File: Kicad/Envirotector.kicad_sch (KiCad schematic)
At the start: 3 parts, among them J1 OLED Display, U1 XIAO-RP2040-DIP, U2 DHT11

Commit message: Upload
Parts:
- added J2: Micro_SD_Card, Connector_Card:microSD_HC_Hirose_DM3AT-SF-PEJM5, symbol Connector:Micro_SD_Card
- added SW1: RotaryEncoder_Switch, Rotary_Encoder:RotaryEncoder_Alps_EC11E-Switch_Vertical_H20mm, symbol Device:RotaryEncoder_Switch
- added U3: ~, LARGE:RTC_DS3231, symbol RTC:RTC_DS3231
- added U4: ~, SPARK:BMP180, symbol BMP:BMP180
- U1: footprint OPL:XIAO-RP2040-DIP -> Module:MOUDLE14P-XIAO-DIP-SMD
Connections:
- net +3.3V: now also J2.4 (VDD), U4.2 (VCC)
- net +5V: now also U3.3 (VCC)
- net GND: now also J2.6 (VSS), J2.9 (SHIELD), SW1.C, SW1.S1, U3.4 (GND), U4.7 (GND)
- net at J1.1 (Pin_1), U1.5 (GPIO6/SDA): now also U3.2 (SDA), U4.6 (SDA)
- net at J1.2 (Pin_2), U1.6 (GPIO7/SCL): now also U3.1 (SCL), U4.5 (SCL)
- net at U1.1 (GPIO26/ADC0/A0): now also J2.2 (DAT3/CD); no longer U2.2 (DATA)
- net at U1.10 (GPIO4/MISO): now also J2.7 (DAT0)
- net at U1.11 (GPIO3/MOSI): now also J2.3 (CMD)
- net at U1.2 (GPIO27/ADC1/A1): now also SW1.S2
- net at U1.3 (GPIO28/ADC2/A2): now also SW1.A
- net at U1.4 (GPIO29/ADC3/A3): now also SW1.B
- net at U1.7 (GPIO0/TX): now also U2.2 (DATA)
- net at U1.9 (GPIO2/SCK): now also J2.5 (CLK)

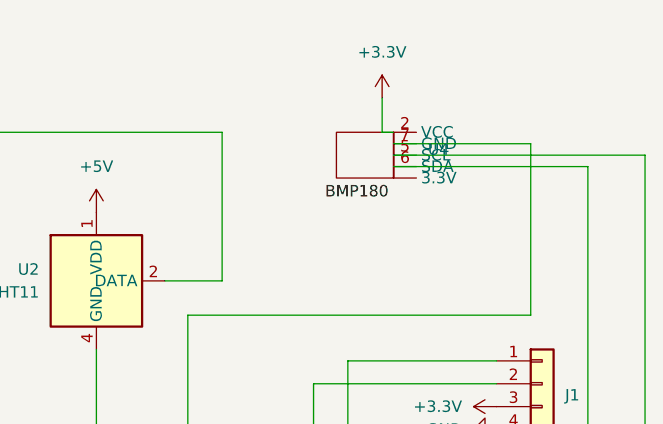
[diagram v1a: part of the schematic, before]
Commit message: updated footprint and case for bmp180 breakout board
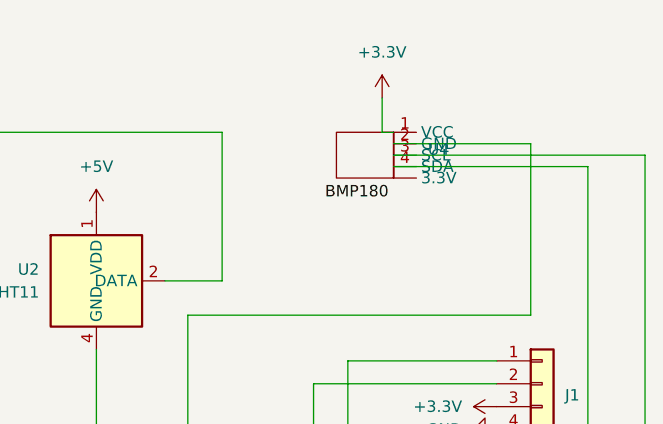
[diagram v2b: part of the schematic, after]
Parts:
- U4: footprint SPARK:BMP180 -> SPARK:Untitled
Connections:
- net +3.3V: now also U4.1 (VCC); no longer U4.2 (VCC)
- net GND: now also U4.2 (GND); no longer U4.7 (GND)
- net at J1.1 (Pin_1), U1.5 (GPIO6/SDA), U3.2 (SDA): now also U4.4 (SDA); no longer U4.6 (SDA)
- net at J1.2 (Pin_2), U1.6 (GPIO7/SCL), U3.1 (SCL): now also U4.3 (SCL); no longer U4.5 (SCL)
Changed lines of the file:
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@@
 			)
 		)
-		(property "Footprint" "SPARK:BMP180"
+		(property "Footprint" "SPARK:Untitled"
 			(at 208.28 38.1 0)
 			(effects
@@
 			)
 		)
-		(pin "5"
+		(pin "1"
 		)
-		(pin "6"
+		(pin "4"
 		)
 		(pin "2"
 		)
-		(pin "7"
+		(pin "3"
 		)
 		(pin ""

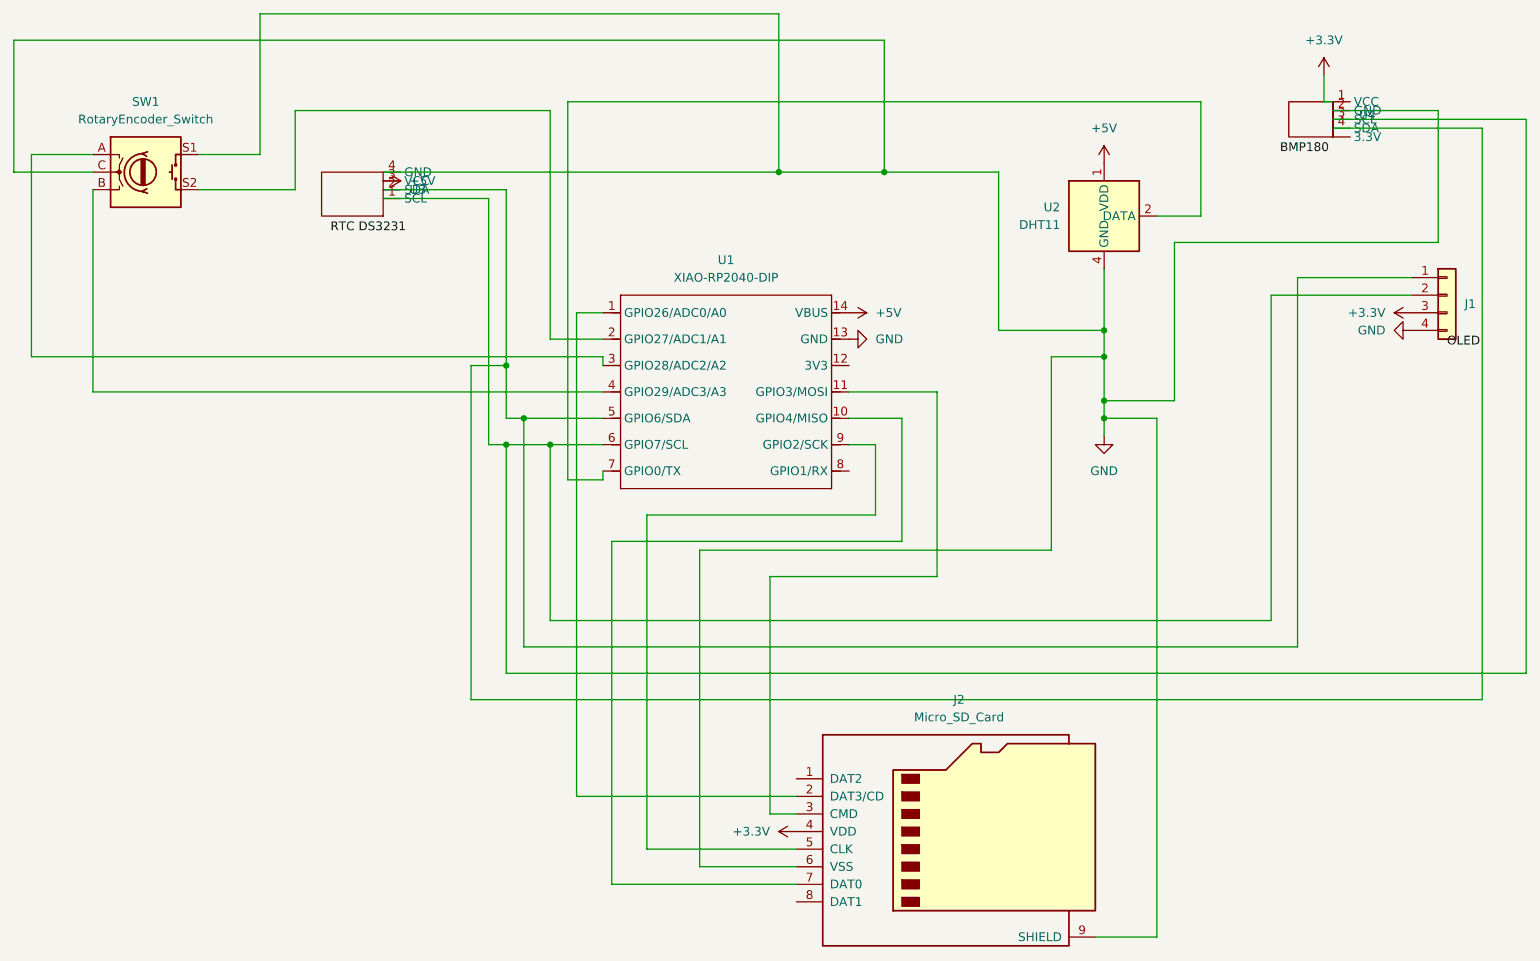
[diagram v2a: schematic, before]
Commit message: updated the sd card reader to breakoutboard
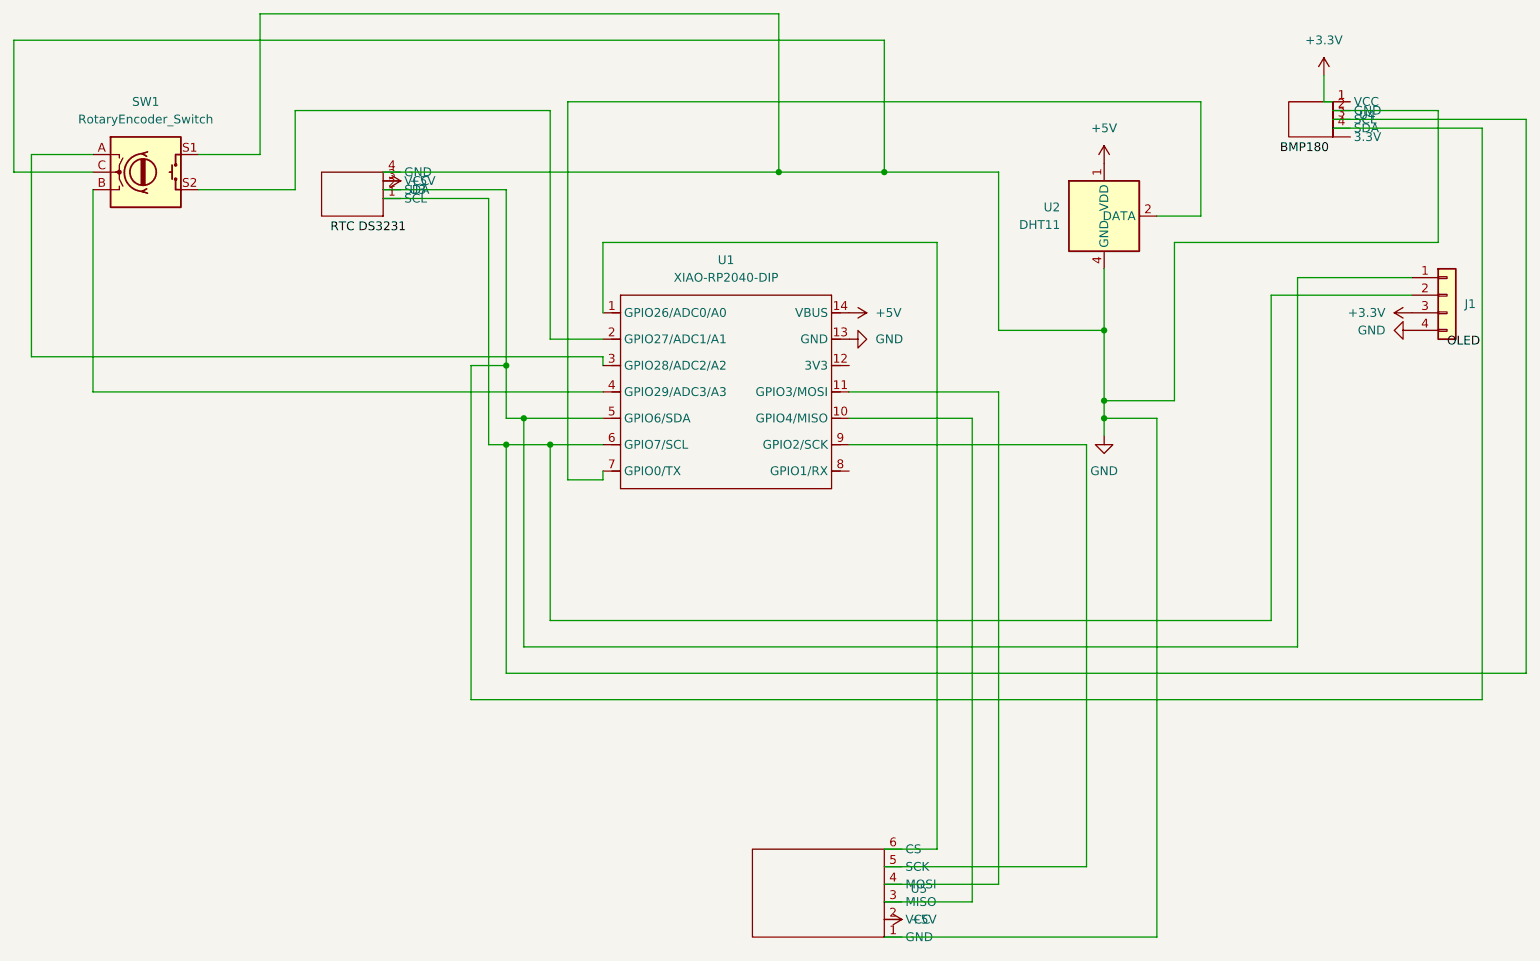
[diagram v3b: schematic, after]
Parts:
- removed J2: Micro_SD_Card, Connector_Card:microSD_HC_Hirose_DM3AT-SF-PEJM5, symbol Connector:Micro_SD_Card
- added U5: ~, SDReader:Untitled, symbol SDReader:SDReader
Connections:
- net +5V: now also U5.2 (VCC)
- net GND: now also U5.1 (GND)
- net at U1.1 (GPIO26/ADC0/A0): now also U5.6 (CS)
- net at U1.11 (GPIO3/MOSI): now also U5.4 (MOSI)
- net at U1.9 (GPIO2/SCK): now also U5.5 (SCK)
- net at U1.10 (GPIO4/MISO): now also U5.3 (MISO)

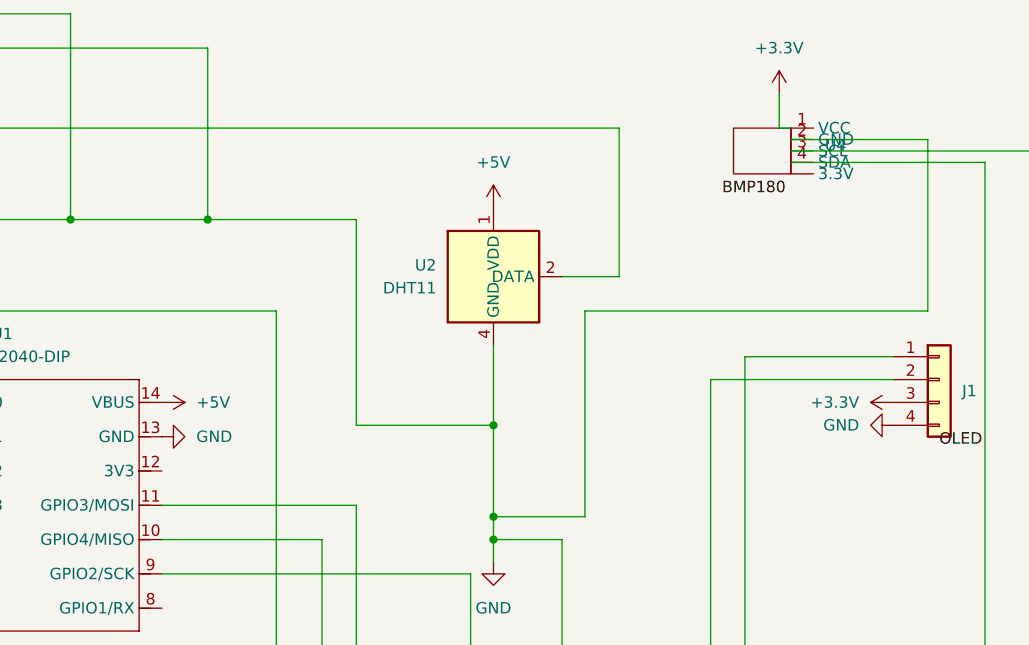
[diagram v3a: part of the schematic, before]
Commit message: updated 3.3v xiao output
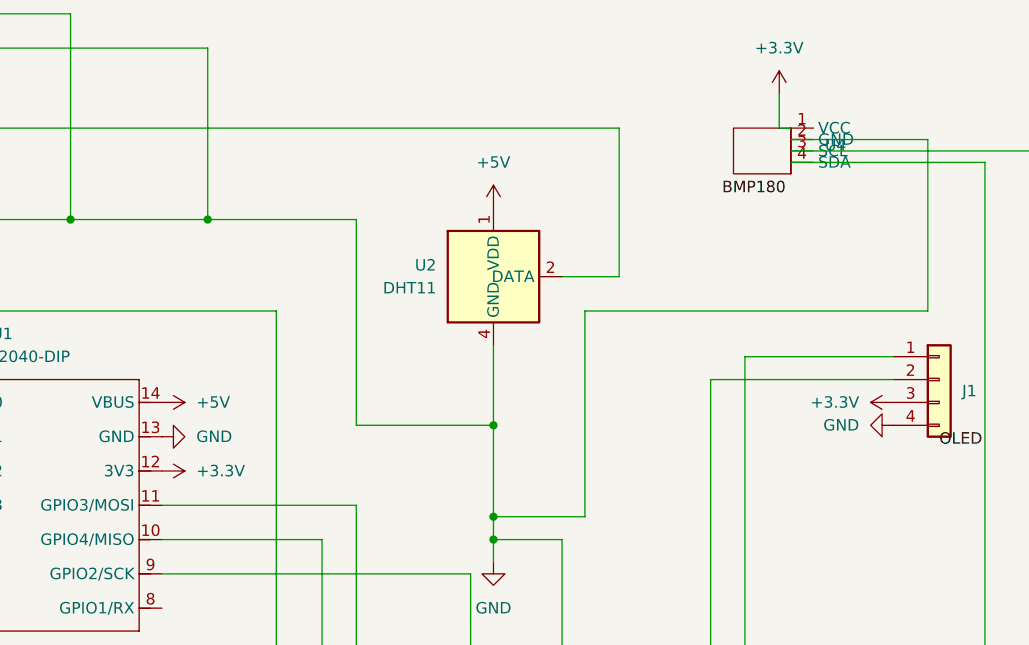
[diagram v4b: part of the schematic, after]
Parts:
- U1: footprint Module:MOUDLE14P-XIAO-DIP-SMD -> OPL:XIAO-RP2040-DIP
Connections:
- net +3.3V: now also U1.12 (3V3)
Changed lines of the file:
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@@
 		(pin "3"
-		)
-		(pin ""
 		)
 		(instances
@@
 			)
 		)
-		(property "Footprint" "Module:MOUDLE14P-XIAO-DIP-SMD"
+		(property "Footprint" "OPL:XIAO-RP2040-DIP"
 			(at 121.158 90.678 0)
 			(effects
@@
 					(unit 1)
 				)
+			)
+		)
+	)
+	(symbol
+		(lib_id "power:+3.3V")
+		(at 138.43 71.12 270)
+		(unit 1)
+		(exclude_from_sim no)
+		(in_bom yes)
+		(on_board yes)
+		(dnp no)
+		(fields_autoplaced yes)
+		(property "Reference" "#PWR09"
+			(at 134.62 71.12 0)
+			(effects
+				(font
+					(size 1.27 1.27)
+				)
+				(hide yes)
+			)
+		)
+		(property "Value" "+3.3V"
+			(at 142.24 71.1199 90)
+			(effects
+				(font
+					(size 1.27 1.27)
+				)
+				(justify left)
+			)
+		)
+		(property "Footprint" ""
+			(at 138.43 71.12 0)
+			(effects
+				(font
+					(size 1.27 1.27)
+				)
+				(hide yes)
+			)
+		)
+		(property "Datasheet" ""
+			(at 138.43 71.12 0)
+			(effects
+				(font
+					(size 1.27 1.27)
+				)
+				(hide yes)
+			)
+		)
+		(property "Description" "Power symbol creates a global label with name \"+3.3V\""
+			(at 138.43 71.12 0)
+			(effects
+				(font
+					(size 1.27 1.27)
+				)
+				(hide yes)
+			)
+		)
+		(pin "1"
+		)
+		(instances
+			(project ""
+				(path "/3f64ad46-f639-46cb-abb5-8c4f16494329"
+					(reference "#PWR09")
+					(unit 1)
+				)
